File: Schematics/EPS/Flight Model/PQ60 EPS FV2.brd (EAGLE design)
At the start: 42 x 42 mm, 55 parts, among them U1 LTC3105EDDPBF, U10 INA3221AIRGVT, U2 LTC3105EDDPBF, U3 LTC3105EDDPBF, U4 LTC4413EDDPBF, U5 LTC4413EDDPBF, U6 TPS63001DRCR, U7 TPS2552DBVT, U8 TPS2552DBVT

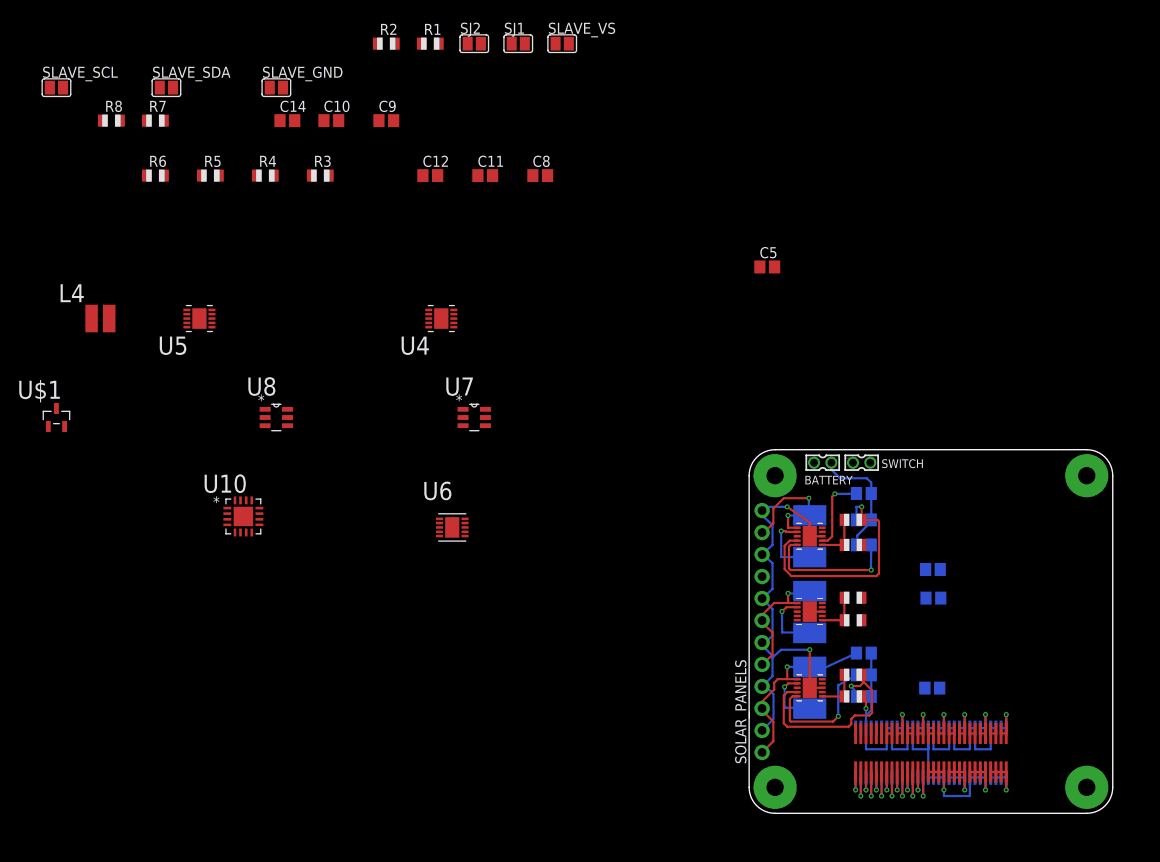
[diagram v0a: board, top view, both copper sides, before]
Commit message: Complteded routing
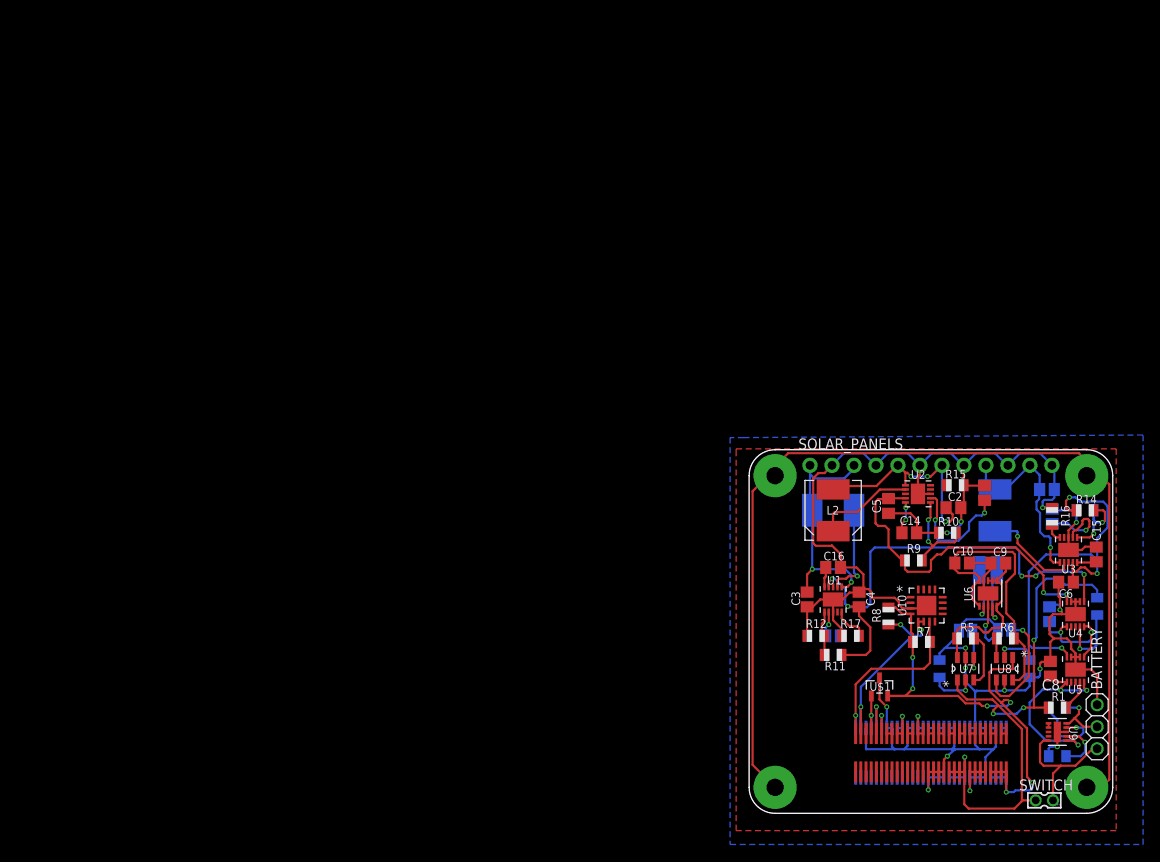
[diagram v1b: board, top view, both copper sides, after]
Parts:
- removed SLAVE_GND, SLAVE_SCL, SLAVE_SDA, SLAVE_VS: (no value), jumper:SJ
- added R15, R16, R17: 466k, adafruit:R0805
- added R18: 487, adafruit:R0805
- added R19: (no value), adafruit:R0805
- added U9: BQ24210DQCT, BQ24210:SON50P200X300X80-11N
- BATTERY: value 332-02 -> (none); device con-garry:332-02 -> adafruit:1X03
- R1, R2: value (none) -> 470k
- moved R6 111.8 mm to (29.6, 20.2), turned to 180 degrees
- moved U5 109.0 mm to (37.7, 16.6), turned to 270 degrees
- moved R7 107.0 mm to (19.9, 19.8)
- moved L4 106.6 mm to (27.6, 28.1), flipped to the bottom
- moved R8 106.4 mm to (16.1, 22.8), turned to 270 degrees
- moved R1 105.5 mm to (35.6, 12.2), turned to 180 degrees
- moved R4 105.1 mm to (32.4, 16.7), flipped to the bottom, turned to 270 degrees
- moved R2 104.7 mm to (40.2, 23.9), flipped to the bottom, turned to 90 degrees
- moved R5 102.3 mm to (25.0, 20.2)
- moved U$1 100.0 mm to (15.1, 14.6)
- moved R3 91.4 mm to (22.0, 16.7), flipped to the bottom, turned to 90 degrees
- moved C10 89.0 mm to (24.6, 28.9), turned to 180 degrees
- moved U8 89.0 mm to (29.5, 16.7), turned to 270 degrees
- moved SJ2 88.4 mm to (25.0, 21.1), flipped to the bottom, turned to 180 degrees
- moved SJ1 88.0 mm to (29.5, 21.2), flipped to the bottom, turned to 180 degrees
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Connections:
- removed net $N70: BATTERY.1, C8.2, SWITCH.1, U5.10, U5.6
- removed net I2C_SCL: R8.2, SLAVE_SCL.1, U10.6
- removed net I2C_SDA: R7.2, SLAVE_SDA.1, U10.7
- removed net N$18: SLAVE_GND.2, SLAVE_SCL.2, SLAVE_SDA.2, SLAVE_VS.2, U10.5
- new net N$28: R15.2, U2.5
- new net N$29: R16.2, U3.5
- new net N$30: R17.2, U1.5
- new net N$31: C8.2, U5.10, U5.6, U9.1
- new net N$32: U9.6, U9.7
- new net N$33: R18.2, U9.2
- new net N$34: BATTERY.1, SWITCH.1, U9.10
- new net N$35: BATTERY.2, R19.2, U9.5
- new net N$36: R19.1, U9.4
- net !RST: now also U$3.P$27
- net +3V3: no longer SLAVE_VS.1
- net BATV: now also SWITCH.2
- net GND: now also BATTERY.3, R15.1, R16.1, R17.1, R18.1, U10.17, U9.11, U9.3; no longer BATTERY.2, SLAVE_GND.1
- net GPIO0: now also U$3.P$25
- net GPIO1: now also U$3.P$26
- net SCL: now also R8.2, U$3.P$29, U10.5, U10.6
- net SDA: now also R7.2, U$3.P$30, U10.7
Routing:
- net CHASSIS_GND: track 0.00 -> 118.4 mm
- net GND: track 147.8 -> 265.8 mm, vias 5 -> 15
- net BATV: track 7.12 -> 69.8 mm, vias 1 -> 4
- net +3V3: track 7.13 -> 62.1 mm, vias 1 -> 6
- net N$6: track 0.00 -> 38.3 mm, vias 0 -> 2
- net UNPROTECTED3V3: track 0.00 -> 33.2 mm
- net N$5: track 24.2 -> 55.7 mm, vias 1 -> 5
- net SCL: track 0.00 -> 25.3 mm, vias 0 -> 3
- net N$31: track 0.00 -> 22.5 mm, vias 0 -> 3
- net SDA: track 0.00 -> 21.5 mm, vias 0 -> 1
- net BATTERY: track 0.00 -> 18.7 mm
- net N$7: track 27.4 -> 45.2 mm, vias 1 -> 3
- net N$34: track 0.00 -> 15.2 mm
- net N$20: track 0.00 -> 14.4 mm, vias 0 -> 2
- net N$23: track 16.0 -> 2.25 mm, vias 1 -> 0
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- added copper zone on layer 1, net GND
- added copper zone on layer 16, net GND

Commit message: many many things
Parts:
- removed R7, R8: 10k, adafruit:R0805
- removed U10: INA3221AIRGVT, INA3221:QFN65P400X400X80-17N
- moved C8 0.10 mm to (34.9, 16.7)
- moved C15 0.05 mm to (40.0, 29.9)
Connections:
- removed net RTN_+3V3_SW1: U$3.P$3, U$3.P$4
- removed net RTN_+3V3_SW2: U$3.P$7, U$3.P$8
- removed net RTN_+3V3_SW3: U$3.P$11, U$3.P$12
- removed net RTN_BATV_SW1: U$3.P$15, U$3.P$16
- removed net RTN_BATV_SW2: U$3.P$19, U$3.P$20
- removed net RTN_BATV_SW3: U$3.P$23, U$3.P$24
- removed net VIN1+: U10.12
- removed net VIN1-: U10.11
- removed net VIN2+: U10.15
- removed net VIN2-: U10.14
- removed net VIN3+: U10.2
- removed net VIN3-: U10.1
- removed net VPU: U10.16
- net +3V3: no longer R7.1, R8.1, U10.4
- net GND: now also U$3.P$11, U$3.P$12, U$3.P$15, U$3.P$16, U$3.P$19, U$3.P$20, U$3.P$23, U$3.P$24, U$3.P$28, U$3.P$3, U$3.P$4, U$3.P$7, U$3.P$8; no longer U10.17, U10.3
- net SCL: no longer R8.2, U10.5, U10.6
- net SDA: no longer R7.2, U10.7
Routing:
- net GND: track 265.8 -> 329.0 mm, vias 15 -> 23
- net SCL: track 25.3 -> 5.12 mm, vias 3 -> 1
- net SDA: track 21.5 -> 3.53 mm
- net +3V3: track 62.1 -> 49.3 mm, vias 6 -> 4
- net MISO: track 0.00 -> 5.13 mm, vias 0 -> 1
- net GPIO8: track 0.00 -> 5.13 mm, vias 0 -> 1
- net GPIO6: track 0.00 -> 5.13 mm, vias 0 -> 1
- net GPIO4: track 0.00 -> 5.13 mm, vias 0 -> 1
- net GPIO2: track 0.00 -> 5.13 mm, vias 0 -> 1
- net GPIO12: track 0.00 -> 5.13 mm, vias 0 -> 1
- net GPIO10: track 0.00 -> 5.13 mm, vias 0 -> 1
- net +3V3_SW3: track 0.60 -> 5.27 mm, vias 0 -> 1
- net MOSI: track 0.00 -> 3.53 mm, vias 0 -> 1
- net BATV_SW1: track 1.20 -> 4.73 mm, vias 0 -> 1
- net SCK: track 0.00 -> 3.53 mm, vias 0 -> 1
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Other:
- board text added: "+"
- board text added: "-"
- board text added: "1"
- board text added: "2"
- board text added: "3"
- board text added: "4"
- board text added: "5"
- board text added: "6"
- board text added: "SASSat EPS FV2"
- board text added: "kartikye.com"
